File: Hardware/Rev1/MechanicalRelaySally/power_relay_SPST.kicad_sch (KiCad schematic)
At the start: 21 parts, among them K1 A31ASQ12VDC2D, U11 DRV120APWR, U12 ACS72981LLRATR-050B3, U13 INA180A1, U14 TLV6001DCK

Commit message: A
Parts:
- D8: footprint Diode_SMD:D_SOD-123 -> Diode_SMD:D_SOD-323F
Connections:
- net CUR_SENSE: no longer U14.3 (-), U14.4
- net IN: now also R10.1
- net OUT: now also U14.3 (-), U14.4
- net at U12.3 (VIOUT): no longer R10.1
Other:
- added sheet VBUF_5V (VBUF_5V.kicad_sch)
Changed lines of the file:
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@@
 	(wire
 		(pts
+			(xy 185.42 30.48) (xy 187.96 30.48)
+		)
+		(stroke
+			(width 0)
+			(type default)
+		)
+	)
+	(wire
+		(pts
 			(xy 208.28 30.48) (xy 198.12 30.48)
 		)
@@
 	(wire
 		(pts
-			(xy 132.08 30.48) (xy 187.96 30.48)
-		)
-		(stroke
-			(width 0)
-			(type default)
-		)
-	)
-	(wire
-		(pts
 			(xy 99.06 25.4) (xy 101.6 25.4)
 		)
@@
 		)
 	)
+	(hierarchical_label "OUT"
+		(shape input)
+		(at 256.54 33.02 0)
+		(effects
+			(font
+				(size 1.27 1.27)
+			)
+			(justify left)
+		)
+	)
 	(hierarchical_label "RELAY_EN"
 		(shape input)
@@
 	(hierarchical_label "CUR_SENSE"
 		(shape input)
-		(at 256.54 33.02 0)
+		(at 260.35 67.31 0)
 		(effects
 			(font
@@
 		)
 	)
-	(rule_area
-		(polyline
-			(pts
-				(xy 187.96 22.86) (xy 215.9 22.86) (xy 215.9 15.24) (xy 248.92 15.24) (xy 255.27 21.59) (xy 255.27 52.07)
-				(xy 195.58 52.07) (xy 187.96 52.07)
-			)
-			(stroke
-				(width 0)
-				(type dash)
-			)
-			(fill
-				(type none)
-			)
-		)
-	)
-	(netclass_flag ""
-		(length 2.54)
-		(shape round)
-		(at 194.31 22.86 0)
+	(hierarchical_label "IN"
+		(shape input)
+		(at 185.42 30.48 180)
 		(effects
 			(font
 				(size 1.27 1.27)
 			)
-			(justify left bottom)
-		)
-		(property "Netclass" ""
-			(at -46.99 -44.45 0)
-			(effects
-				(font
-					(size 1.27 1.27)
-				)
-			)
-		)
-		(property "Component Class" "SINGLE_VBUF2"
-			(at 195.072 20.32 0)
-			(effects
-				(font
-					(size 1.27 1.27)
-					(italic yes)
-				)
-				(justify left)
-			)
+			(justify right)
 		)
 	)
@@
 			)
 		)
-		(property "Footprint" "Diode_SMD:D_SOD-123"
+		(property "Footprint" "Diode_SMD:D_SOD-323F"
 			(at 219.71 36.83 0)
 			(effects
@@
 				)
 			)
+		)
+	)
+	(sheet
+		(at 234.95 80.01)
+		(size 19.05 10.16)
+		(exclude_from_sim no)
+		(in_bom yes)
+		(on_board yes)
+		(dnp no)
+		(fields_autoplaced yes)
+		(stroke
+			(width 0.1524)
+			(type solid)
+		)
+		(fill
+			(color 255 255 194 1.0000)
+		)
+		(property "Sheetname" "VBUF_5V"
+			(at 234.95 79.2984 0)
+			(effects
+				(font
+					(size 1.27 1.27)
+				)
+				(justify left bottom)
+			)
+		)
+		(property "Sheetfile" "VBUF_5V.kicad_sch"
+			(at 234.95 90.7546 0)
+			(effects
+				(font
+					(size 1.27 1.27)
+				)
+				(justify left top)
+			)
+		)
+		(pin "IN" input
+			(at 254 82.55 0)
+			(effects
+				(font
+					(size 1.27 1.27)
+				)
+				(justify right)
+			)
+		)
+		(pin "OUT" input
+			(at 254 85.09 0)
+			(effects
+				(font
+					(size 1.27 1.27)
+				)
+				(justify right)
+			)
+		)
+		(instances
+			(project "MechanicalRelaySally"
+				(path "/fc3bfb83-1db4-4bd1-b480-85f699496fec/82deb2ae-220f-4425-88c6-a1e80ead50b8/c4275d10-fe67-4c10-b169-dea82861b062"
+					(page "10")
+				)
+			)

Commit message: A
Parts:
- removed C8: 100n, Capacitor_SMD:C_0402_1005Metric, symbol Device:C
- removed U14: TLV6001DCK, Package_TO_SOT_SMD:SOT-353_SC-70-5, symbol Amplifier_Operational:TLV6001DCK
- renumbered C6 to C5, C7 to C6, U11 to U10, U12 to U11, U13 to U12
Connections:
- net CUR_SENSE: now also C6.1, D8.1 (K), R10.2, R11.2
- net IN: no longer R10.1
- net at U11.3 (VIOUT): now also R10.1
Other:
- removed sheet VBUF_5V

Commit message: A
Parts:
- removed C6: 100n, Capacitor_SMD:C_0402_1005Metric, symbol Device:C
- removed D8: 5V, Diode_SMD:D_SOD-323F, symbol Device:D_Zener
- removed R10: 100k, Resistor_SMD:R_0603_1608Metric, symbol Device:R
- removed R11: 195k, Resistor_SMD:R_0603_1608Metric, symbol Device:R
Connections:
- net CUR_SENSE: now also U11.3 (VIOUT)

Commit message: A
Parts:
- added C4, C46: 100n, Capacitor_SMD:C_0402_1005Metric, symbol Device:C
- added D2, D44: 5V, Diode_SMD:D_SOD-323F, symbol Device:D_Zener
- added R1, R75: 10k, Resistor_SMD:R_0603_1608Metric, symbol Device:R
- added R2, R81: 18k, Resistor_SMD:R_0603_1608Metric, symbol Device:R
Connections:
- net COIL_CUR: now also C46.1, D44.1 (K), R75.2, R81.2; no longer U12.1
- net CUR_SENSE: now also C4.1, D2.1 (K), R1.2, R2.2; no longer U11.3 (VIOUT)
- net GND: now also C4.2, C46.2, D2.2 (A), D44.2 (A), R2.1, R81.1
- new net: R75.1, U12.1
- new net: R1.1, U11.3 (VIOUT)

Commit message: a
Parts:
- K1: value A31ASQ12VDC2D -> A31ASP12VDC2D; Part# 2449-A31ASQ12VDC2D-ND -> 2449-A31ASP12VDC2D-ND
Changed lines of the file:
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@@
 			)
 		)
-		(property "Value" "A31ASQ12VDC2D"
+		(property "Value" "A31ASP12VDC2D"
 			(at 134.62 43.18 0)
 			(effects
@@
 			)
 		)
-		(property "Part#" "2449-A31ASQ12VDC2D-ND"
+		(property "Part#" "2449-A31ASP12VDC2D-ND"
 			(at 134.366 44.45 0)
 			(effects

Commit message: Added subs for comps
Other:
- note added: "Substitute 200k"
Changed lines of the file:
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@@
+		)
+	)
+	(text "Substitute 200k"
+		(exclude_from_sim no)
+		(at 154.94 138.684 0)
+		(effects
+			(font
+				(size 1.27 1.27)
+				(color 255 0 0 1)
+			)
 		)
 	)

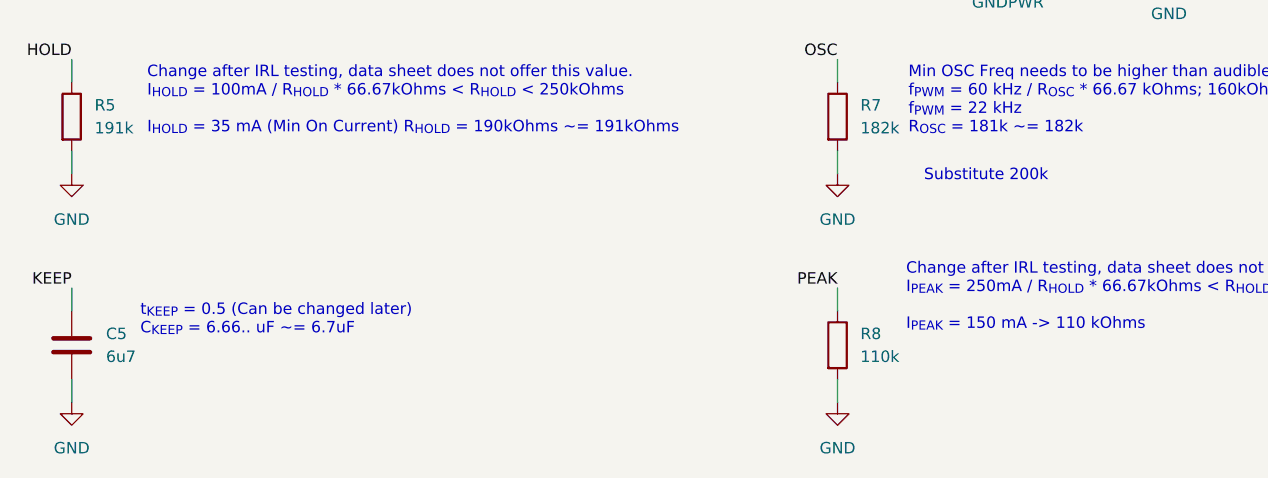
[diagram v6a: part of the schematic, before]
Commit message: Fixed the issue and found that relay diode and foot print were wrong see schematic for spdt for details rev 1.
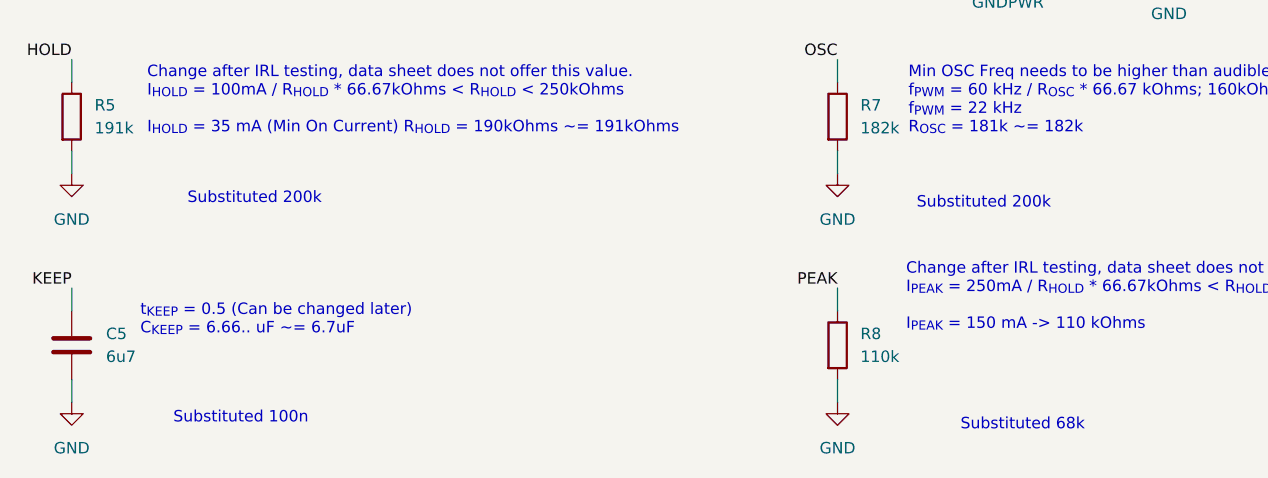
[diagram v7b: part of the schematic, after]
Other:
- note added: "Substituted 100n"
- note added: "Substituted 200k"
- note added: "Substituted 68k"
- note removed: "Substitute 200k"

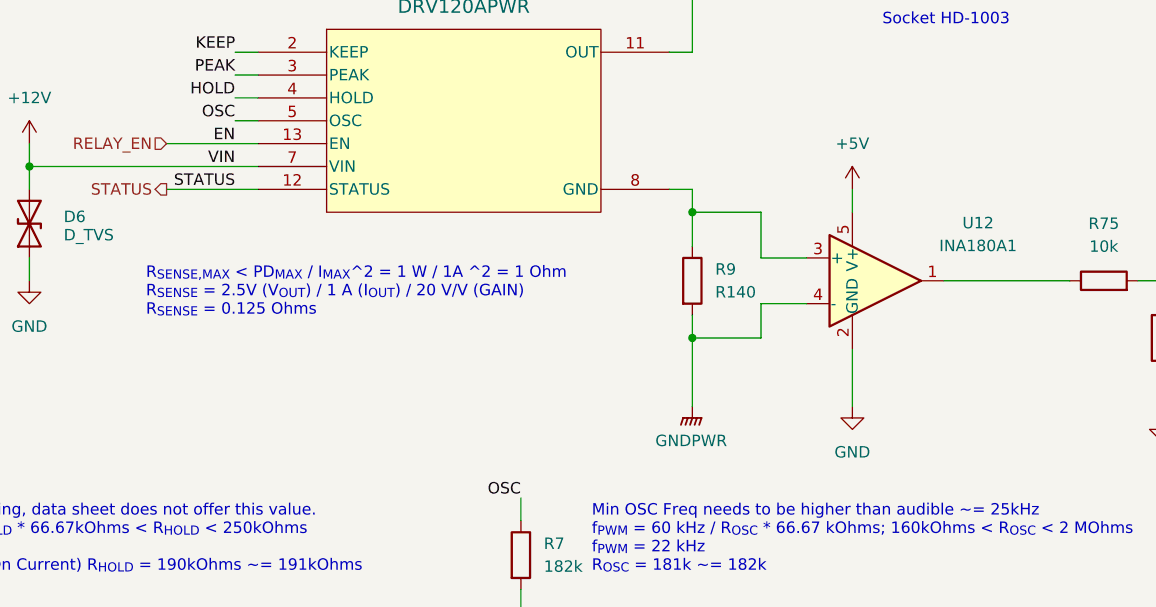
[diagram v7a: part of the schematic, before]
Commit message: figured out relay current monitoring is wrong
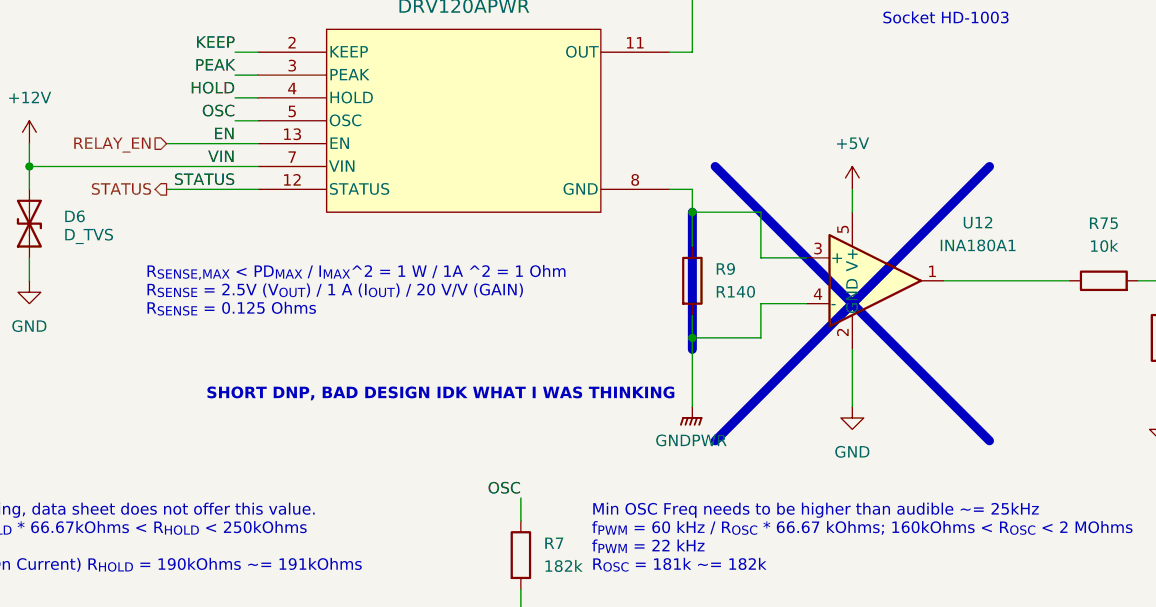
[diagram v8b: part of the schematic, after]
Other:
- note added: "SHORT DNP, BAD DESIGN IDK WHAT I WAS THINKING"
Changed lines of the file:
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@@
+		)
+	)
+	(text "SHORT DNP, BAD DESIGN IDK WHAT I WAS THINKING"
+		(exclude_from_sim no)
+		(at 129.54 114.3 0)
+		(effects
+			(font
+				(size 1.27 1.27)
+				(thickness 0.254)
+				(bold yes)
+				(color 255 0 0 1)
+			)
 		)
 	)
@@
 		)
 	)
+	(polyline
+		(pts
+			(xy 160.02 88.9) (xy 190.5 119.38)
+		)
+		(stroke
+			(width 1)
+			(type solid)
+			(color 255 0 0 1)
+		)
+	)
 	(wire
 		(pts
@@
 		)
 	)
+	(polyline
+		(pts
+			(xy 160.02 119.38) (xy 190.5 88.9)
+		)
+		(stroke
+			(width 1)
+			(type solid)
+			(color 255 0 0 1)
+		)
+	)
 	(wire
 		(pts
@@
 		)
 	)
+	(polyline
+		(pts
+			(xy 157.48 93.98) (xy 157.48 109.22)
+		)
+		(stroke
+			(width 1)
+			(type solid)
+			(color 255 0 0 1)
+		)
+	)
